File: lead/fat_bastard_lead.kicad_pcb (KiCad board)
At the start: 2 copper layers, 180 x 35 mm, 40 parts, among them J1 LD_12V, J2 LD_IN, J3 LD_GAIN, J4 LD_OUT, J5 HT_IN, U1 ECC83, U2 ECC83

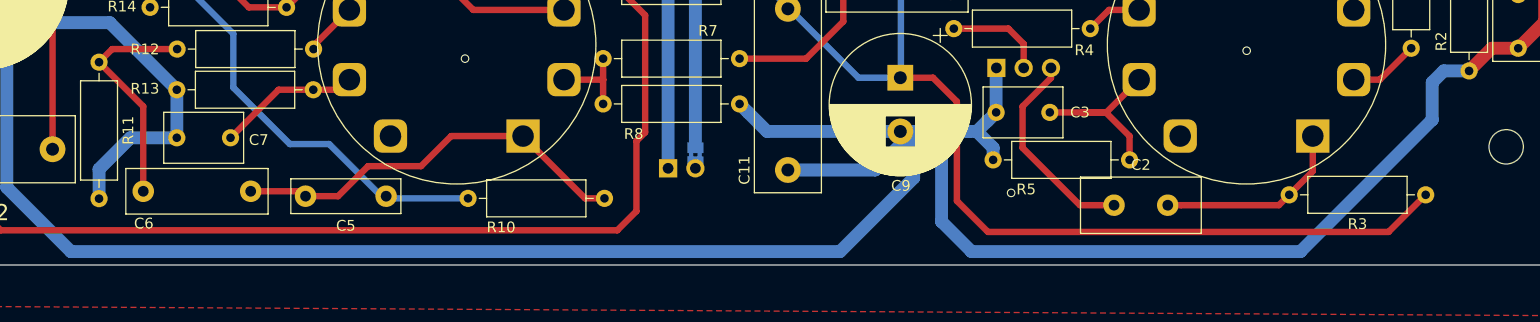
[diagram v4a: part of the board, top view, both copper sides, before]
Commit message: [lead] change footprint for C2
C2 is currently a 500p capacitor, doing heavy filtering of the low
frequencies to achieve a "modern" tone. By changing the footprint, it
can be replaced with a film capacitor (i.e. MKS4) of up to 10nF, giving
a broader range of possible tones.
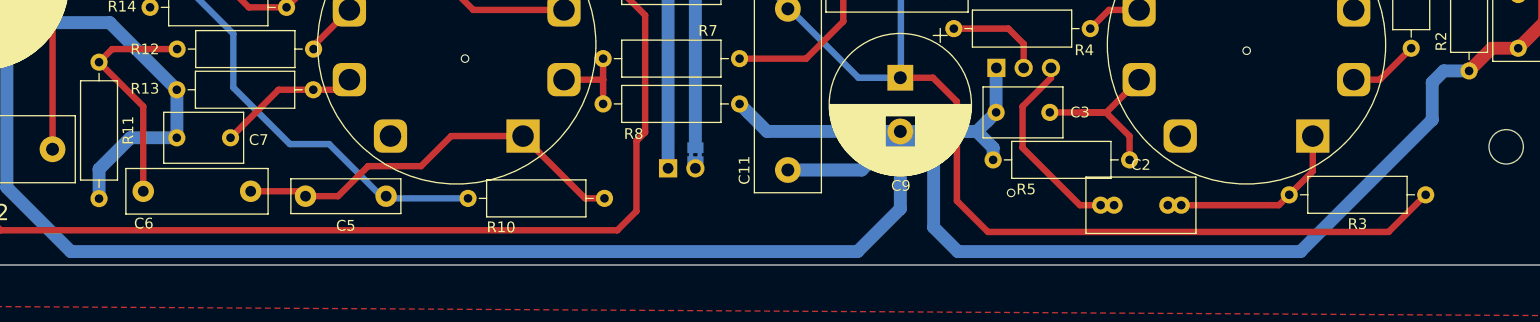
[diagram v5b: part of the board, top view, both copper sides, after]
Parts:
- C2: footprint Capacitor_THT:C_Disc_D11.0mm_W5.0mm_P5.00mm -> Capacitor_THT:C_Rect_L10.0mm_W5.0mm_P5.00mm_P7.50mm
- moved C2 1.24 mm to (197.3, 89.4)
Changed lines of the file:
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@@
-  )
-  (module Capacitor_THT:C_Disc_D11.0mm_W5.0mm_P5.00mm (layer F.Cu)
-    (at 198.501 89.4334)
-    (descr "C, Disc series, Radial, pin pitch=5.00mm, , diameter*width=11*5.0mm^2, Capacitor, http://www.vishay.com/docs/28535/vy2series.pdf")
-    (tags "C Disc series Radial pin pitch 5.00mm  diameter 11mm width 5.0mm Capacitor")
-    (fp_text reference C2 (at 2.5 -3.75) (layer F.SilkS)
-      (effects (font (size 1 1) (thickness 0.15)))
-    )
-    (fp_text value 500p (at 2.5 3.75) (layer F.Fab)
-      (effects (font (size 1 1) (thickness 0.15)))
-    )
-    (fp_text user %R (at 2.5 0) (layer F.Fab)
-      (effects (font (size 1 1) (thickness 0.15)))
-    )
-    (fp_line (start 8.25 -2.75) (end -3.25 -2.75) (layer F.CrtYd) (width 0.05))
-    (fp_line (start 8.25 2.75) (end 8.25 -2.75) (layer F.CrtYd) (width 0.05))
-    (fp_line (start -3.25 2.75) (end 8.25 2.75) (layer F.CrtYd) (width 0.05))
-    (fp_line (start -3.25 -2.75) (end -3.25 2.75) (layer F.CrtYd) (width 0.05))
-    (fp_line (start 8.12 -2.62) (end 8.12 2.62) (layer F.SilkS) (width 0.12))
-    (fp_line (start -3.12 -2.62) (end -3.12 2.62) (layer F.SilkS) (width 0.12))
-    (fp_line (start -3.12 2.62) (end 8.12 2.62) (layer F.SilkS) (width 0.12))
-    (fp_line (start -3.12 -2.62) (end 8.12 -2.62) (layer F.SilkS) (width 0.12))
-    (fp_line (start 8 -2.5) (end -3 -2.5) (layer F.Fab) (width 0.1))
-    (fp_line (start 8 2.5) (end 8 -2.5) (layer F.Fab) (width 0.1))
-    (fp_line (start -3 2.5) (end 8 2.5) (layer F.Fab) (width 0.1))
-    (fp_line (start -3 -2.5) (end -3 2.5) (layer F.Fab) (width 0.1))
-    (pad 2 thru_hole circle (at 5 0) (size 2 2) (drill 1) (layers *.Cu *.Mask)
-      (net 4 /HT1))
-    (pad 1 thru_hole circle (at 0 0) (size 2 2) (drill 1) (layers *.Cu *.Mask)
-      (net 3 "Net-(C2-Pad1)"))
-    (model ${KISYS3DMOD}/Capacitor_THT.3dshapes/C_Disc_D11.0mm_W5.0mm_P5.00mm.wrl
-      (at (xyz 0 0 0))
-      (scale (xyz 1 1 1))
-      (rotate (xyz 0 0 0))
-    )
   )
   (module Capacitor_THT:C_Disc_D11.0mm_W5.0mm_P5.00mm (layer F.Cu)
@@
       (xy -2.549664 1.91989) (xy -2.469928 1.911165) (xy -2.400256 1.919918)) (layer F.SilkS) (width 0.01))
   )
+  (module Capacitor_THT:C_Rect_L10.0mm_W5.0mm_P5.00mm_P7.50mm (layer F.Cu)
+    (at 197.2564 89.4334)
+    (descr "C, Rect series, Radial, pin pitch=5.00mm 7.50mm, , length*width=10*5mm^2, Capacitor")
+    (tags "C Rect series Radial pin pitch 5.00mm 7.50mm  length 10mm width 5mm Capacitor")
+    (fp_text reference C2 (at 3.75 -3.75) (layer F.SilkS)
+      (effects (font (size 1 1) (thickness 0.15)))
+    )
+    (fp_text value 500p (at 3.75 3.75) (layer F.Fab)
+      (effects (font (size 1 1) (thickness 0.15)))
+    )
+    (fp_line (start -1.25 -2.5) (end -1.25 2.5) (layer F.Fab) (width 0.1))
+    (fp_line (start -1.25 2.5) (end 8.75 2.5) (layer F.Fab) (width 0.1))
+    (fp_line (start 8.75 2.5) (end 8.75 -2.5) (layer F.Fab) (width 0.1))
+    (fp_line (start 8.75 -2.5) (end -1.25 -2.5) (layer F.Fab) (width 0.1))
+    (fp_line (start -1.37 -2.62) (end 8.87 -2.62) (layer F.SilkS) (width 0.12))
+    (fp_line (start -1.37 2.62) (end 8.87 2.62) (layer F.SilkS) (width 0.12))
+    (fp_line (start -1.37 -2.62) (end -1.37 2.62) (layer F.SilkS) (width 0.12))
+    (fp_line (start 8.87 -2.62) (end 8.87 2.62) (layer F.SilkS) (width 0.12))
+    (fp_line (start -1.5 -2.75) (end -1.5 2.75) (layer F.CrtYd) (width 0.05))
+    (fp_line (start -1.5 2.75) (end 9 2.75) (layer F.CrtYd) (width 0.05))
+    (fp_line (start 9 2.75) (end 9 -2.75) (layer F.CrtYd) (width 0.05))
+    (fp_line (start 9 -2.75) (end -1.5 -2.75) (layer F.CrtYd) (width 0.05))
+    (fp_text user %R (at 2.5 0) (layer F.Fab)
+      (effects (font (size 1 1) (thickness 0.15)))
+    )
+    (pad 1 thru_hole circle (at 1.25 0) (size 1.6 1.6) (drill 0.8) (layers *.Cu *.Mask)
+      (net 3 "Net-(C2-Pad1)"))
+    (pad 2 thru_hole circle (at 6.25 0) (size 1.6 1.6) (drill 0.8) (layers *.Cu *.Mask)
+      (net 4 /HT1))
+    (pad 1 thru_hole circle (at 0 0) (size 1.6 1.6) (drill 0.8) (layers *.Cu *.Mask)
+      (net 3 "Net-(C2-Pad1)"))
+    (pad 2 thru_hole circle (at 7.5 0) (size 1.6 1.6) (drill 0.8) (layers *.Cu *.Mask)
+      (net 4 /HT1))
+    (model ${KISYS3DMOD}/Capacitor_THT.3dshapes/C_Rect_L10.0mm_W5.0mm_P5.00mm_P7.50mm.wrl
+      (at (xyz 0 0 0))
+      (scale (xyz 1 1 1))
+      (rotate (xyz 0 0 0))
+    )
+  )
   (gr_line (start 239 95) (end 239 79) (layer F.CrtYd) (width 0.2))
   (gr_line (start 231 95) (end 239 95) (layer F.CrtYd) (width 0.2))
@@
   (segment (start 77.5716 69.596) (end 72.1322 69.596) (width 1.2) (layer B.Cu) (net 1))
   (segment (start 87.1036 78.4352) (end 93.091 72.4478) (width 1.2) (layer B.Cu) (net 1))
-  (segment (start 95.4532 87.7824) (end 95.4532 74.81) (width 1.2) (layer B.Cu) (net 1))
-  (segment (start 101.42079 93.74999) (end 95.4532 87.7824) (width 1.2) (layer B.Cu) (net 1))
-  (segment (start 95.4532 74.81) (end 93.091 72.4478) (width 1.2) (layer B.Cu) (net 1))
-  (segment (start 173.00081 93.74999) (end 101.42079 93.74999) (width 1.2) (layer B.Cu) (net 1))
-  (segment (start 179.8574 82.5716) (end 179.8574 86.8934) (width 1.2) (layer B.Cu) (net 1))
-  (segment (start 179.8574 86.8934) (end 173.00081 93.74999) (width 1.2) (layer B.Cu) (net 1))
   (segment (start 79.5256 87.9856) (end 77.54 86) (width 1.2) (layer B.Cu) (net 1))
   (segment (start 85.6234 87.9856) (end 79.5256 87.9856) (width 1.2) (layer B.Cu) (net 1))
@@
   (segment (start 179.8574 82.5716) (end 166.2138 82.5716) (width 1.2) (layer B.Cu) (net 1))
   (segment (start 166.2138 82.5716) (end 164.452199 80.809999) (width 1.2) (layer B.Cu) (net 1))
-  (segment (start 176.2722 86.1568) (end 179.8574 82.5716) (width 1.2) (layer B.Cu) (net 1))
-  (segment (start 168.148 86.1568) (end 176.2722 86.1568) (width 1.2) (layer B.Cu) (net 1))
   (segment (start 184.9844 82.5716) (end 179.8574 82.5716) (width 1.2) (layer B.Cu) (net 1))
   (segment (start 187.2488 85.217) (end 187.2488 84.08563) (width 1.2) (layer B.Cu) (net 1))
@@
   (segment (start 233.6546 74.8284) (end 231.5464 76.9366) (width 1.2) (layer F.Cu) (net 1))
   (segment (start 236.1184 74.8284) (end 233.6546 74.8284) (width 1.2) (layer F.Cu) (net 1))
-  (segment (start 229.1842 76.9366) (end 231.5464 76.9366) (width 1.2) (layer B.Cu) (net 1))
-  (segment (start 228.1174 78.0034) (end 229.1842 76.9366) (width 1.2) (layer B.Cu) (net 1))
-  (segment (start 182.4482 85.1624) (end 182.4482 90.9574) (width 1.2) (layer B.Cu) (net 1))
-  (segment (start 179.8574 82.5716) (end 182.4482 85.1624) (width 1.2) (layer B.Cu) (net 1))
-  (segment (start 182.4482 90.9574) (end 185.24079 93.74999) (width 1.2) (layer B.Cu) (net 1))
-  (segment (start 215.85061 93.74999) (end 228.1174 81.4832) (width 1.2) (layer B.Cu) (net 1))
-  (segment (start 185.24079 93.74999) (end 215.85061 93.74999) (width 1.2) (layer B.Cu) (net 1))
-  (segment (start 228.1174 81.4832) (end 228.1174 78.0034) (width 1.2) (layer B.Cu) (net 1))
   (segment (start 104.0384 88.8238) (end 104.0384 86.0806) (width 1.2) (layer B.Cu) (net 1))
   (segment (start 106.9594 83.1596) (end 111.2774 83.1596) (width 1.2) (layer B.Cu) (net 1))
@@
   (segment (start 86.3416 79.1972) (end 87.1036 78.4352) (width 1.2) (layer B.Cu) (net 1))
   (segment (start 81.3562 79.1972) (end 86.3416 79.1972) (width 1.2) (layer B.Cu) (net 1))
+  (segment (start 95.4532 74.81) (end 93.091 72.4478) (width 1.2) (layer B.Cu) (net 1))
+  (segment (start 101.42079 93.74999) (end 95.4532 87.7824) (width 1.2) (layer B.Cu) (net 1))
+  (segment (start 174.62641 93.74999) (end 101.42079 93.74999) (width 1.2) (layer B.Cu) (net 1))
+  (segment (start 178.6128 82.5716) (end 178.6128 89.7636) (width 1.2) (layer B.Cu) (net 1))
+  (segment (start 95.4532 87.7824) (end 95.4532 74.81) (width 1.2) (layer B.Cu) (net 1))
+  (segment (start 178.6128 89.7636) (end 174.62641 93.74999) (width 1.2) (layer B.Cu) (net 1))
+  (segment (start 181.7116 85.6704) (end 178.6128 82.5716) (width 1.2) (layer B.Cu) (net 1))
+  (segment (start 181.7116 91.4908) (end 181.7116 85.6704) (width 1.2) (layer B.Cu) (net 1))
+  (segment (start 229.1842 76.9366) (end 228.1174 78.0034) (width 1.2) (layer B.Cu) (net 1))
+  (segment (start 231.5464 76.9366) (end 229.1842 76.9366) (width 1.2) (layer B.Cu) (net 1))
+  (segment (start 228.1174 78.0034) (end 228.1174 81.4832) (width 1.2) (layer B.Cu) (net 1))
+  (segment (start 228.1174 81.4832) (end 215.85061 93.74999) (width 1.2) (layer B.Cu) (net 1))
+  (segment (start 215.85061 93.74999) (end 183.97079 93.74999) (width 1.2) (layer B.Cu) (net 1))
+  (segment (start 183.97079 93.74999) (end 181.7116 91.4908) (width 1.2) (layer B.Cu) (net 1))
+  (segment (start 175.0276 86.1568) (end 178.6128 82.5716) (width 1.2) (layer B.Cu) (net 1))
+  (segment (start 168.148 86.1568) (end 175.0276 86.1568) (width 1.2) (layer B.Cu) (net 1))
   (segment (start 231.5464 64.2366) (end 227.8126 67.9704) (width 0.6) (layer F.Cu) (net 2))
   (segment (start 224.0996 67.9704) (end 220.81 71.26) (width 0.6) (layer F.Cu) (net 2))
@@
   (segment (start 217 86.276) (end 214.8078 88.4682) (width 0.6) (layer F.Cu) (net 4))
   (segment (start 217 83) (end 217 86.276) (width 0.6) (layer F.Cu) (net 4))
-  (segment (start 203.5064 89.4334) (end 204.7564 89.4334) (width 0.6) (layer F.Cu) (net 4))
   (segment (start 213.8426 89.4334) (end 214.8078 88.4682) (width 0.6) (layer F.Cu) (net 4))
   (segment (start 204.7564 89.4334) (end 213.8426 89.4334) (width 0.6) (layer F.Cu) (net 4))
+  (segment (start 203.5064 89.4334) (end 204.7564 89.4334) (width 0.6) (layer F.Cu) (net 4))
   (segment (start 192.5282 80.7974) (end 195.5292 80.7974) (width 0.6) (layer F.Cu) (net 5))
   (segment (start 197.7926 80.7974) (end 200.84 77.75) (width 0.6) (layer F.Cu) (net 5))

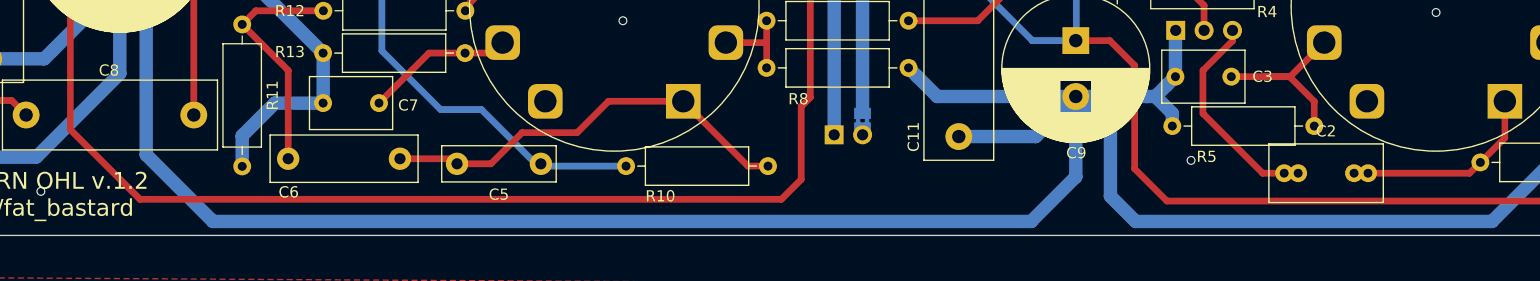
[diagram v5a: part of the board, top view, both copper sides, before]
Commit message: Add alternate component values for guitar
In its original form, this preamp could very well be used with a guitar,
providing a rather tight and modern sound.

This patch adds alternate values, designed for use with guitar,
resulting in a warmer, fuller, stoner/rock guitar tone.

Signed-off-by: Arnaud Ferraris <arnaud.ferraris@gmail.com>
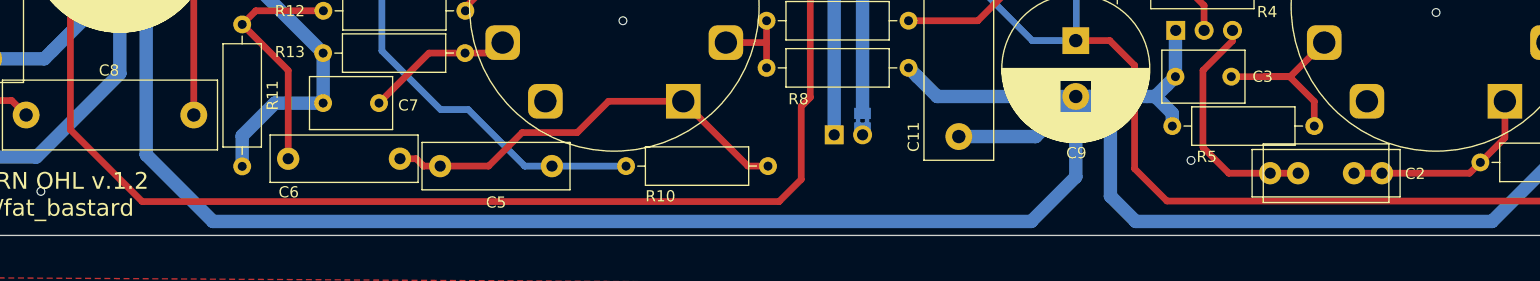
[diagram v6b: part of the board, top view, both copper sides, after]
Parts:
- added REF**: C_Rect_L13.0mm_W4.0mm_P10.00mm_FKS3_FKP3_MKS4, Capacitor_THT:C_Rect_L13.0mm_W4.0mm_P10.00mm_FKS3_FKP3_MKS4, F.Cu at (196.0, 89.4)
- C13: value 500p -> 360p
- C2: footprint Capacitor_THT:C_Rect_L10.0mm_W5.0mm_P5.00mm_P7.50mm -> Capacitor_THT:C_Disc_D11.0mm_W5.0mm_P5.00mm
- C5: footprint Capacitor_THT:C_Rect_L10.0mm_W3.0mm_P7.50mm_MKS4 -> Capacitor_THT:C_Rect_L13.0mm_W4.0mm_P10.00mm_FKS3_FKP3_MKS4
- moved C2 1.25 mm to (198.5, 89.4)
- moved C5 1.01 mm to (131.7, 88.8)
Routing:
- net Net-(C2-Pad1): track 19.3 -> 21.0 mm
